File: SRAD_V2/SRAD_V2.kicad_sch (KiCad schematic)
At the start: 46 parts, among them J1 Conn_01x04_Pin, J3 RSP-122811-02, J7 691210910002, U1 STM32F767ZIT6, U12 MAX-M10S, U13 MS5607-02BA, U14 MMC5983MA, U17 AS5F31G04SND-08LIN, U4 LSM6DSV80XTR

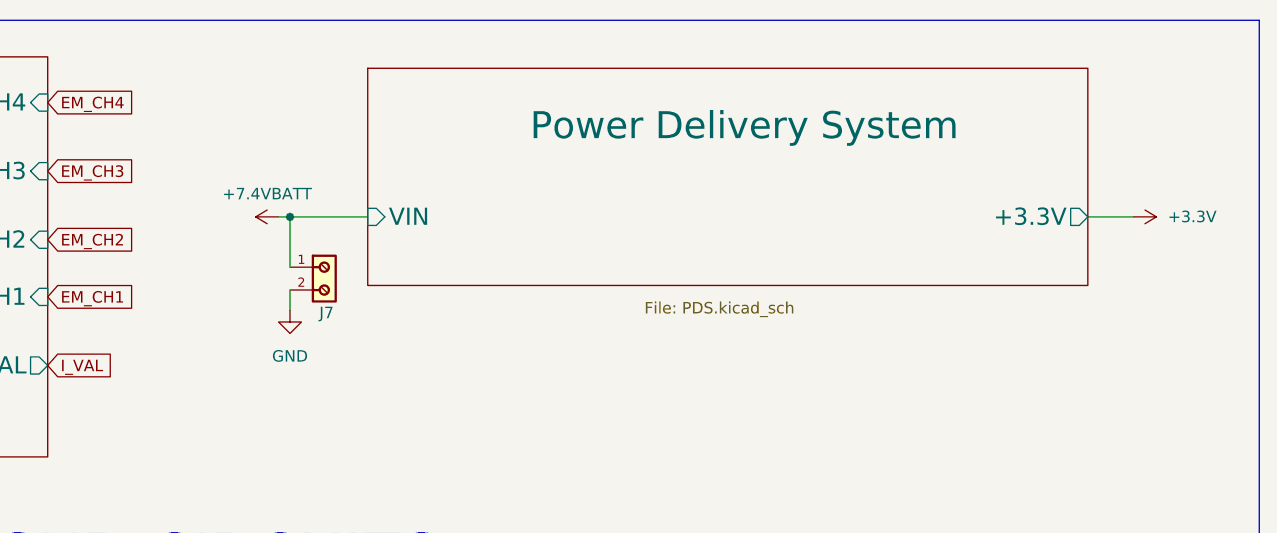
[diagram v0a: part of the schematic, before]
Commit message: added reverse polarity protection
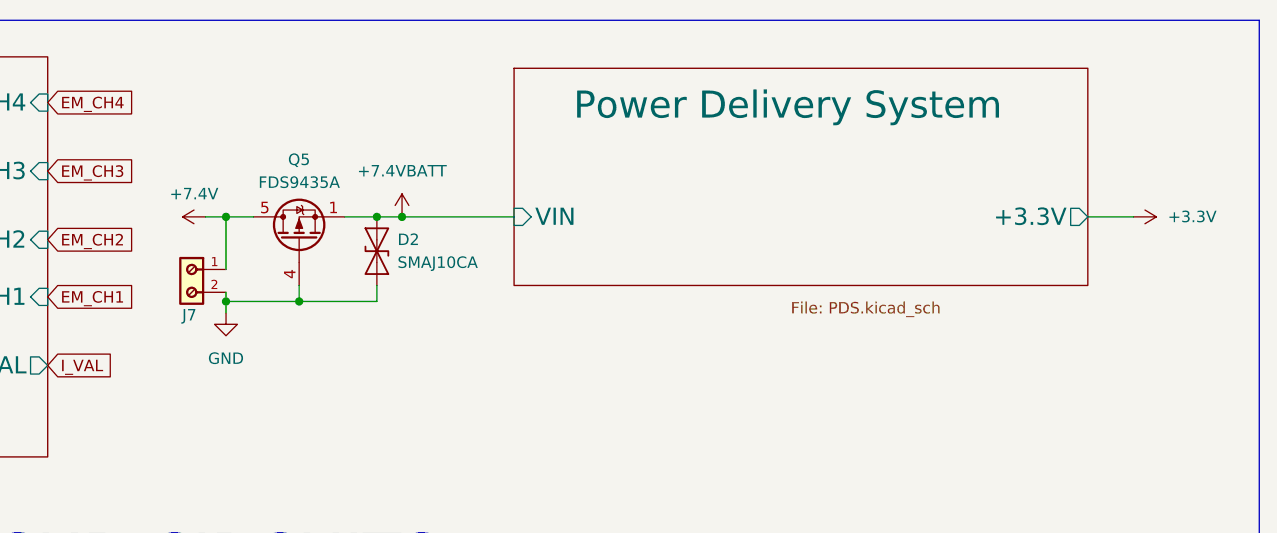
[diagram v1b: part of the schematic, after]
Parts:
- added D2: SMAJ10CA, Diode_SMD:D_SMA, symbol Diode:SMAJ10CA
- added Q5: FDS9435A, Package_SO:SOIC-8_3.9x4.9mm_P1.27mm, symbol Transistor_FET:FDS9435A
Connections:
- net +7.4VBATT: now also D2.2 (A2), Q5.1 (S), Q5.2 (S), Q5.3 (S); no longer J7.1
- net GND: now also D2.1 (A1), Q5.4 (G)
- new net +7.4V: J7.1, Q5.5 (D), Q5.6 (D), Q5.7 (D), Q5.8 (D)
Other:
- moved on the sheet: J7

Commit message: Focusing on signal integrity and shielding now!
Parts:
- removed FB2: FerriteBead_Small, symbol Device:FerriteBead_Small
- removed Q5: FDS9435A, Package_SO:SOIC-8_3.9x4.9mm_P1.27mm, symbol Transistor_FET:FDS9435A
- added D3: SMAJ10CA, Diode_SMD:D_SMA, symbol Diode:SMAJ10CA
- added D4: MBRA340, Diode_SMD:D_SMA, symbol Diode:MBRA340
- added J4: Micro_SD_Card, Connector_Card:microSD_HC_Hirose_DM3D-SF, symbol Connector:Micro_SD_Card
- added J6: 691210910002, Screw_Terminal:691210910002, symbol Screw Terminal:691210910002
- C22: footprint Capacitor_SMD:C_0603_1608Metric -> Capacitor_SMD:C_1210_3225Metric
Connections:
- net +3.3V: now also J4.4 (VDD)
- net +3.7VBATT: now also D3.2 (A2), J6.1
- net +7.4V: now also D2.2 (A2), D4.2 (A)
- net +7.4VBATT: now also D4.1 (K); no longer D2.2 (A2)
- net GND: now also D3.1 (A1), J4.6 (VSS), J4.SH (SHIELD), J6.2
- net SDMMC2_CK: now reaches U1.122 (PD6)
- net SDMMC2_CK: now also J4.5 (CLK)
- net SDMMC2_CMD: now reaches U1.123 (PD7)
- net SDMMC2_CMD: now also J4.3 (CMD)
- net SDMMC2_D2: now reaches U1.126 (PG11)
- net SDMMC2_D2: now also J4.1 (DAT2)
- net SDMMC2_D3: now reaches U1.127 (PG12)
- net SDMMC2_D3: now also J4.2 (DAT3/CD)
- net SDMMC2_D0: now reaches U1.75 (PB14)
- net SDMMC2_D0: now also J4.7 (DAT0)
- net SDMMC2_D1: now reaches U1.76 (PB15)
- net SDMMC2_D1: now also J4.8 (DAT1)
- no-connect marks 7 -> 6
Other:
- note added: "MAGNETOMETER"
- note added: "MICRO SD CARD SLOT"
- note added: "Needs a TVS diode?"
- note added: "Reverse voltage protection"
- note removed: "MAGNOMETER"
- company: (none) -> Author: Gundeep Sidhu
- moved on the sheet: BZ2, D2

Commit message: Layout optimisation
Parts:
- removed D2, D3: SMAJ10CA, Diode_SMD:D_SMA, symbol Diode:SMAJ10CA
- removed J4: Micro_SD_Card, Connector_Card:microSD_HC_Hirose_DM3D-SF, symbol Connector:Micro_SD_Card
- added C40, C41: 10p, symbol Device:C_Small
- added D5, D6: SD05C-01F, Diode_SMD:D_SOD-323, symbol Diode:SD05C-01F
- added D7, D8: MBR1020VL, Diode_SMD:D_SOD-123F, symbol Diode:MBR1020VL
- added J4: USB_C_Receptacle_USB2.0_16P, Connector_USB:USB_C_Receptacle_GCT_USB4105-xx-A_16P_TopMnt_Horizontal, symbol Connector:USB_C_Receptacle_USB2.0_16P
- added R14, R15: 5k1, symbol Device:R_Small
- added R16: 4.7k, symbol Device:R_Small
- added TP1: TestPoint, symbol Connector:TestPoint
- added Y1: Crystal, Crystal:Crystal_SMD_0603-2Pin_6.0x3.5mm, symbol Device:Crystal
- C21, C23, C24: footprint Capacitor_SMD:C_0603_1608Metric -> Capacitor_SMD:C_0402_1005Metric
- C35: footprint Capacitor_SMD:C_0603_1608Metric -> Capacitor_SMD:C_1210_3225Metric
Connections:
- net +3.3V: now also J1.4 (Pin_4), TP1.1; no longer J1.3 (Pin_3)
- net +3.7VBATT: now also D7.1 (K)
- net +7.4V: now also D8.1 (K)
- net GND: now also J1.2 (Pin_2), C40.2, C41.2, D5.1 (A1), D6.1 (A1), D7.2 (A), D8.2 (A), J4.A1 (GND), J4.A12 (GND), J4.B1 (GND), J4.B12 (GND), J4.SH (SHIELD), R14.2, R15.2; no longer J1.4 (Pin_4)
- net IMU_SPI_CS: now also U1.96 (PC6); no longer U1.100 (PA8)
- net MAG_SPI_CS: now also U1.97 (PC7); no longer U1.101 (PA9)
- net SWCLK: now also J1.3 (Pin_3); no longer J1.2 (Pin_2)
- net USB_OTG_FS_DM: now reaches U1.103 (PA11)
- net USB_OTG_FS_DM: now also D6.2 (A2), J4.A7 (D-), J4.B7 (D-)
- net USB_OTG_FS_DP: now reaches U1.104 (PA12)
- net USB_OTG_FS_DP: now also D5.2 (A2), J4.A6 (D+), J4.B6 (D+)
- net RCC_OSC_IN: now reaches U1.23 (PH0)
- net RCC_OSC_IN: now also C40.1, Y1.2
- net RCC_OSC_OUT: now reaches U1.24 (PH1)
- net RCC_OSC_OUT: now also C41.1, Y1.1
- net BAROMETER_SI renamed BAROMETER_MOSI
- net BAROMETER_SO renamed BAROMETER_MISO
- net SDMMC2_CK: no longer names the net of U1.122 (PD6)
- net SDMMC2_CMD: no longer names the net of U1.123 (PD7)
- net SDMMC2_D0: no longer names the net of U1.75 (PB14)
- net SDMMC2_D1: no longer names the net of U1.76 (PB15)
- net SDMMC2_D2: no longer names the net of U1.126 (PG11)
- net SDMMC2_D3: no longer names the net of U1.127 (PG12)
- new net: J4.B5 (CC2), R14.1
- new net: J4.A5 (CC1), R15.1
- new net USB_OTG_FS_VBUS: J4.A4 (VBUS), J4.A9 (VBUS), J4.B4 (VBUS), J4.B9 (VBUS), U1.101 (PA9)
- no-connect marks 6 -> 8
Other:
- note added: "25MHz"
- note added: "48MHz - is configurable in the MCU"
- note added: "Depends on the protocol"
- note added: "Differential Pair"
- note added: "MCU needs an external crystal oscillator of 25MHz"
- note added: "USB-C"
- note removed: "MICRO SD CARD SLOT"
- note removed: "Needs a TVS diode?"
- moved on the sheet: BZ2, D4, J6, J7

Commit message: Layout almost finalised!
Only thing left is to connect and layout parts of the GPS and antenna! This was after changing the layer stackup from SGPS to SGGS with power being routed on the top giving seamless ground planes providing EMI protection and signal integrity to signals being routed via vias :)
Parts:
- removed TP1: TestPoint, symbol Connector:TestPoint
- removed Y1: Crystal, Crystal:Crystal_SMD_0603-2Pin_6.0x3.5mm, symbol Device:Crystal
- added AE1: GP.1575.18.4.A.02, GP-1575-18-4-A-02:ANT_GP.1575.18.4.A.02_TAL, symbol GP-1575-18-4-A-02:GP.1575.18.4.A.02
- added C42: 100n, Capacitor_SMD:C_0402_1005Metric_Pad0.74x0.62mm_HandSolder, symbol Device:C_Small
- added JP1: SolderJumper_2_Open, Jumper:SolderJumper-2_P1.3mm_Open_RoundedPad1.0x1.5mm, symbol Jumper:SolderJumper_2_Open
- added R17: 10k, Resistor_SMD:R_0402_1005Metric_Pad0.72x0.64mm_HandSolder, symbol Device:R_Small
- added R18: 4.7k, Resistor_SMD:R_0402_1005Metric_Pad0.72x0.64mm_HandSolder, symbol Device:R_Small
- added X1: Crystal, VXM7_9032_25M0000000:VXM7_MCH, symbol Crystal Osc:VXM7-9032-25M0000000
- C40, C41: value 10p -> 12p; footprint (none) -> Capacitor_SMD:C_0402_1005Metric
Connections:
- net +3.3V: now also C42.1, JP1.2 (B)
- net GND: now also C42.2, R17.2, X1.2, X1.4
- net RCC_OSC_IN: now also X1.3
- net RCC_OSC_OUT: now also X1.1
- net USB_OTG_FS_VBUS: now also R17.1, R18.2; no longer J4.A4 (VBUS), J4.A9 (VBUS), J4.B4 (VBUS), J4.B9 (VBUS)
- net at J3.1 (SIGNAL), L2.2, U12.11 (RF_IN): now also AE1.1
- net USB_OTG_FS_DM renamed USB_OTG_FS_D-
- net USB_OTG_FS_DP renamed USB_OTG_FS_D+
- new net Power Delivery System/+3.3V: JP1.1 (A)
- new net USB_5V: J4.A4 (VBUS), J4.A9 (VBUS), J4.B4 (VBUS), J4.B9 (VBUS), R18.1
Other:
- moved on the sheet: C35, C40, C41, D4, D8, J7

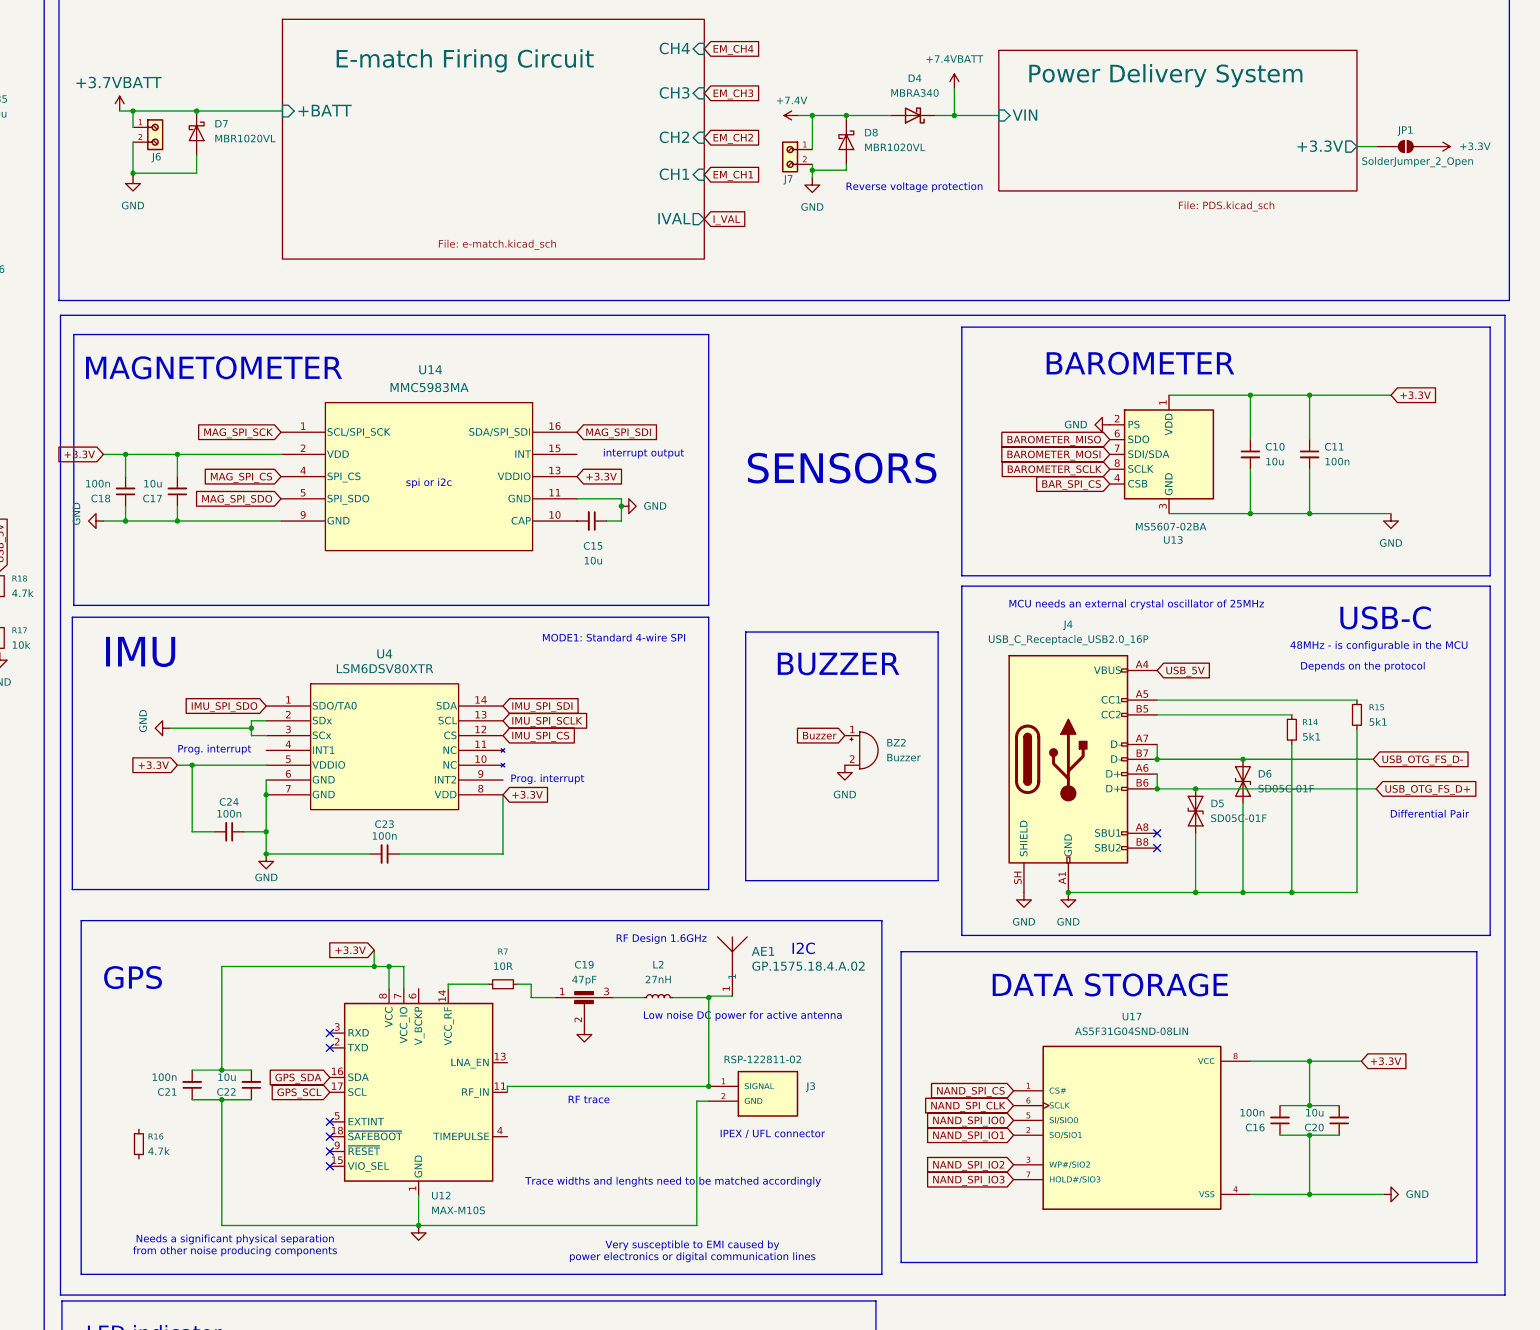
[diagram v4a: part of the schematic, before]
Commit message: ensuring proper grounding in the layout
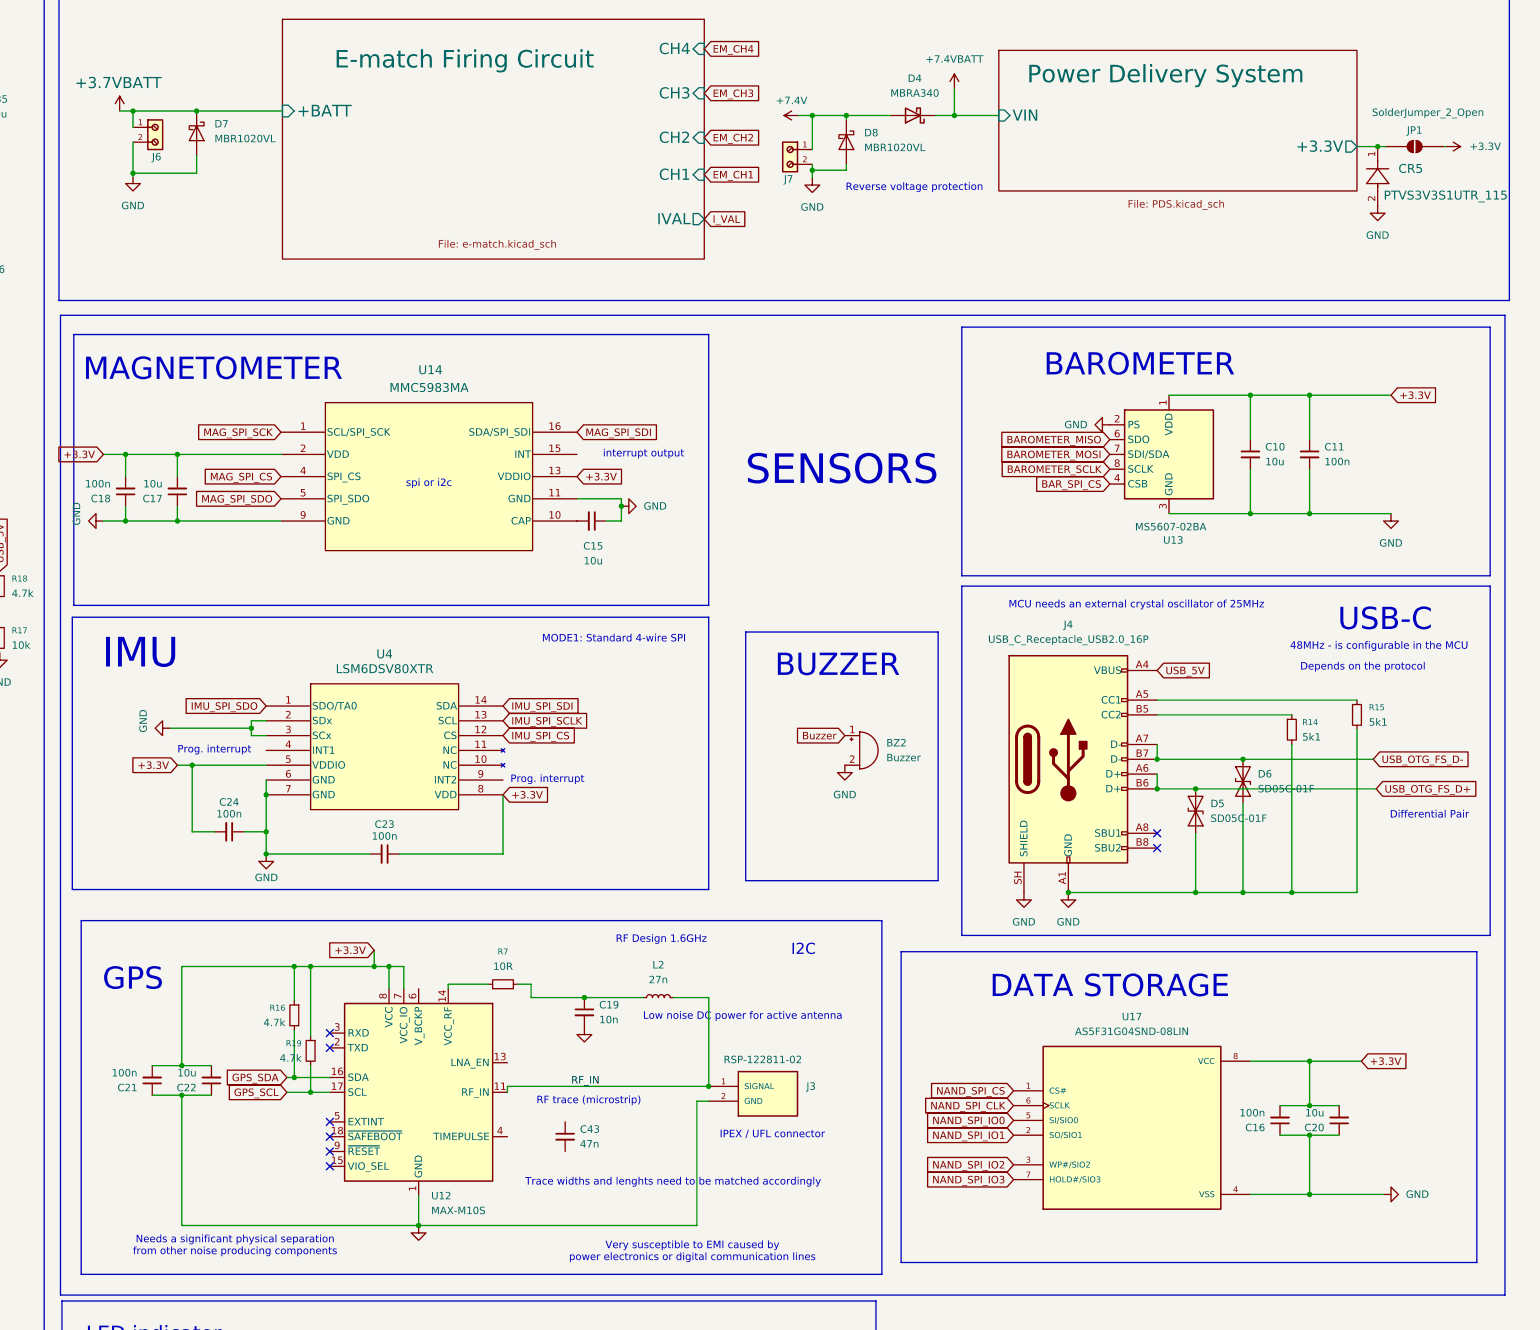
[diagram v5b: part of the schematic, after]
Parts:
- removed AE1: GP.1575.18.4.A.02, GP-1575-18-4-A-02:ANT_GP.1575.18.4.A.02_TAL, symbol GP-1575-18-4-A-02:GP.1575.18.4.A.02
- removed C19: 47pF, symbol Device:C_Feedthrough
- added C19: 10n, Capacitor_SMD:C_0402_1005Metric, symbol Device:C_Small
- added C43: 47n, Capacitor_SMD:C_0402_1005Metric, symbol Device:C_Small
- added CR5: PTVS3V3S1UTR_115, PTVS3V3S1UTR_115:CR_PTVS3V_NEX-L, symbol PTVS3V3S1UTR_115:PTVS3V3S1UTR_115
- added R19: 4.7k, Resistor_SMD:R_0402_1005Metric_Pad0.72x0.64mm_HandSolder, symbol Device:R_Small
- L2: value 27nH -> 27n; footprint (none) -> Inductor_SMD:L_0402_1005Metric
- R16: footprint (none) -> Resistor_SMD:R_0402_1005Metric_Pad0.72x0.64mm_HandSolder
- R7: footprint (none) -> Resistor_SMD:R_0402_1005Metric
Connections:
- net +3.3V: now also R16.1, R19.1
- net GND: now also C19.2, CR5.2
- net GPS_SCL: now also R19.2
- net GPS_SDA: now also R16.2
- net Power Delivery System/+3.3V: now also CR5.1
- net RF_IN: now reaches J3.1 (SIGNAL), L2.2, U12.11 (RF_IN)
- net at L2.1: now also R7.2, C19.1
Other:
- note added: "RF trace (microstrip)"
- note removed: "RF trace"
- moved on the sheet: C21, C22, JP1, R16

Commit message: Updated IMU sensor and generated Interactive BOM using a plugin
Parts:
- removed C10, C20: 10u, Capacitor_SMD:C_0603_1608Metric, symbol Device:C_Small
- removed U4: LSM6DSV80XTR, MMC5983MA:MMC5983MA_MEM, symbol LSM6DSV80XTR:LSM6DSV80XTR
- added C44: 47pF, Capacitor_SMD:C_0402_1005Metric, symbol Device:C_Small
- added C45, C46, C47: 1u, Capacitor_SMD:C_0603_1608Metric, symbol Device:C_Small
- added Q6: MMBT3904, Package_TO_SOT_SMD:SOT-23, symbol Transistor_BJT:MMBT3904
- added R21: 4.7k, Resistor_SMD:R_0603_1608Metric, symbol Device:R_Small
- added R22, R23: 806R, Resistor_SMD:R_0603_1608Metric, symbol Device:R_Small
- added U5: LSM6DSVTR, LGA14-L_2P59X3P1X0P5_STM, symbol LSM6DSVTR:LSM6DSVTR
- BZ2: footprint Buzzer_Beeper:MagneticBuzzer_StarMicronics_HMB-06_HMB-12 -> Buzzer_Beeper:Buzzer_12x9.5RM7.6
- C15: footprint Capacitor_SMD:C_0402_1005Metric_Pad0.74x0.62mm_HandSolder -> Capacitor_SMD:C_1206_3216Metric
- C17: value 10u -> 1u; footprint Capacitor_SMD:C_0402_1005Metric_Pad0.74x0.62mm_HandSolder -> Capacitor_SMD:C_0603_1608Metric
- C18, C25, C26, C27, C28, C29, C30, C31, C32, C33, C34, C39, C42: footprint Capacitor_SMD:C_0402_1005Metric_Pad0.74x0.62mm_HandSolder -> Capacitor_SMD:C_0603_1608Metric
- C21, C23, C24: footprint Capacitor_SMD:C_0402_1005Metric -> Capacitor_SMD:C_0603_1608Metric
- C22, C35: footprint Capacitor_SMD:C_1210_3225Metric -> Capacitor_SMD:C_1206_3216Metric
- C43, J6: now not fitted; now left out of the parts list
- R13: value 1k -> 806R
- R14, R15: value 5k1 -> 4.7k; footprint (none) -> Resistor_SMD:R_0603_1608Metric
- R16, R17, R18, R19: footprint Resistor_SMD:R_0402_1005Metric_Pad0.72x0.64mm_HandSolder -> Resistor_SMD:R_0603_1608Metric
- R7: footprint Resistor_SMD:R_0402_1005Metric -> Resistor_SMD:R_1206_3216Metric
- R8: footprint (none) -> Resistor_SMD:R_0603_1608Metric
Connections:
- net +3.3V: now also BZ2.1 (+), C45.1, C46.1, C47.2, U5.5 (VDD_IO), U5.8 (VDD)
- net Buzzer: now also R21.1, R22.1, R23.1; no longer BZ2.1 (+)
- net GND: now also C45.2, C46.2, C47.1, Q6.2 (E), R21.2, U5.2 (SDX), U5.3 (SCX), U5.7 (GND); no longer BZ2.2 (-)
- net IMU_SPI_CS: now also U5.12 (CS)
- net IMU_SPI_SCLK: now also U5.13 (SCL)
- net IMU_SPI_SDI: now also U5.14 (SDA)
- net IMU_SPI_SDO: now also U5.1 (SDO/SA0)
- net NAND_SPI_CS: now also U1.63 (PE10); no longer U1.69 (PB10)
- net RF_IN: now also C44.1; no longer J3.1 (SIGNAL), L2.2
- new net: BZ2.2 (-), Q6.3 (C)
- new net: C44.2, J3.1 (SIGNAL), L2.2
- new net: Q6.1 (B), R22.2, R23.2
- no-connect marks 8 -> 10
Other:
- note added: "Critical length = 19.05 cm / 12 = 1.587cm"
- note added: "DC Block Cap"
- note added: "Eff. Res. = 400ohms BOM Consolidation"
- note added: "Trace widths and lengths need to be matched accordingly"
- note added: "approx 2mA of current"
- note removed: "Trace widths and lenghts need to be matched accordingly"
- note removed: "approx 1.4mA of current"
- moved on the sheet: BZ2, C11, C16, C19, C21, C22, J3, L2, R16, R19, R7, U12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
